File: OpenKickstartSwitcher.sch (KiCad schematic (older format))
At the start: 12 parts, among them J1 Conn_01x03, J2 Conn_01x03, J99 OSHW_LOGO, U1 KS_SOCKET, U2 M27C800, U3 7400

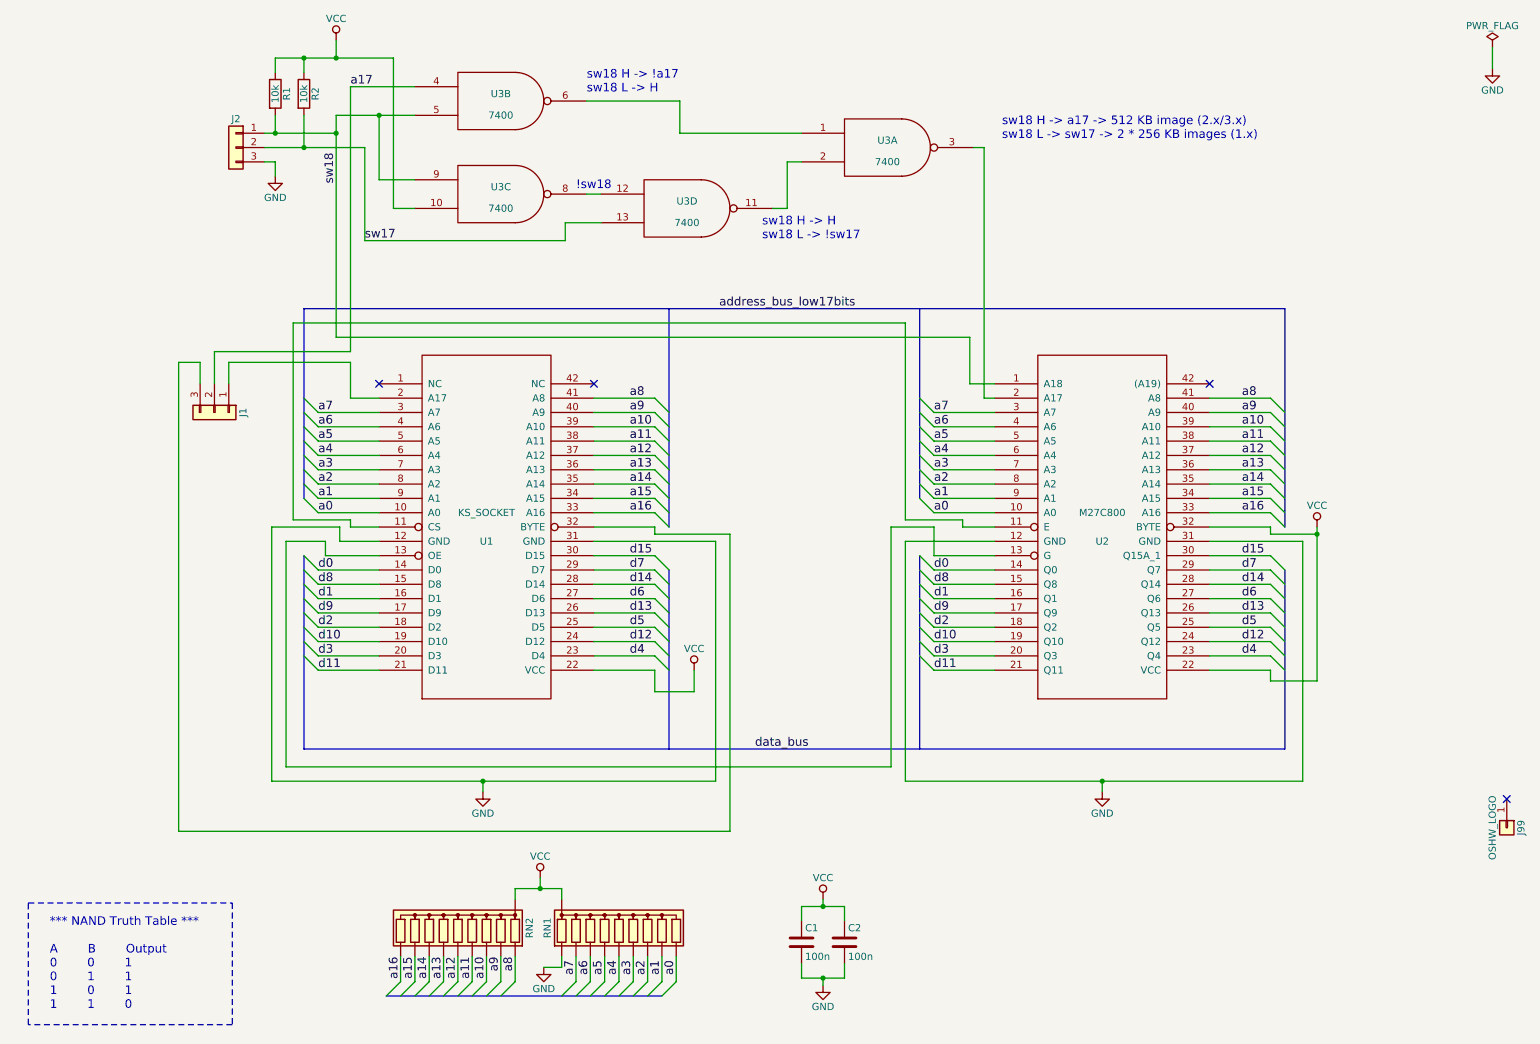
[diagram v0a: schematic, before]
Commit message: Tentative schematics for 5-kickstart version PCB NOT YET UPDATED
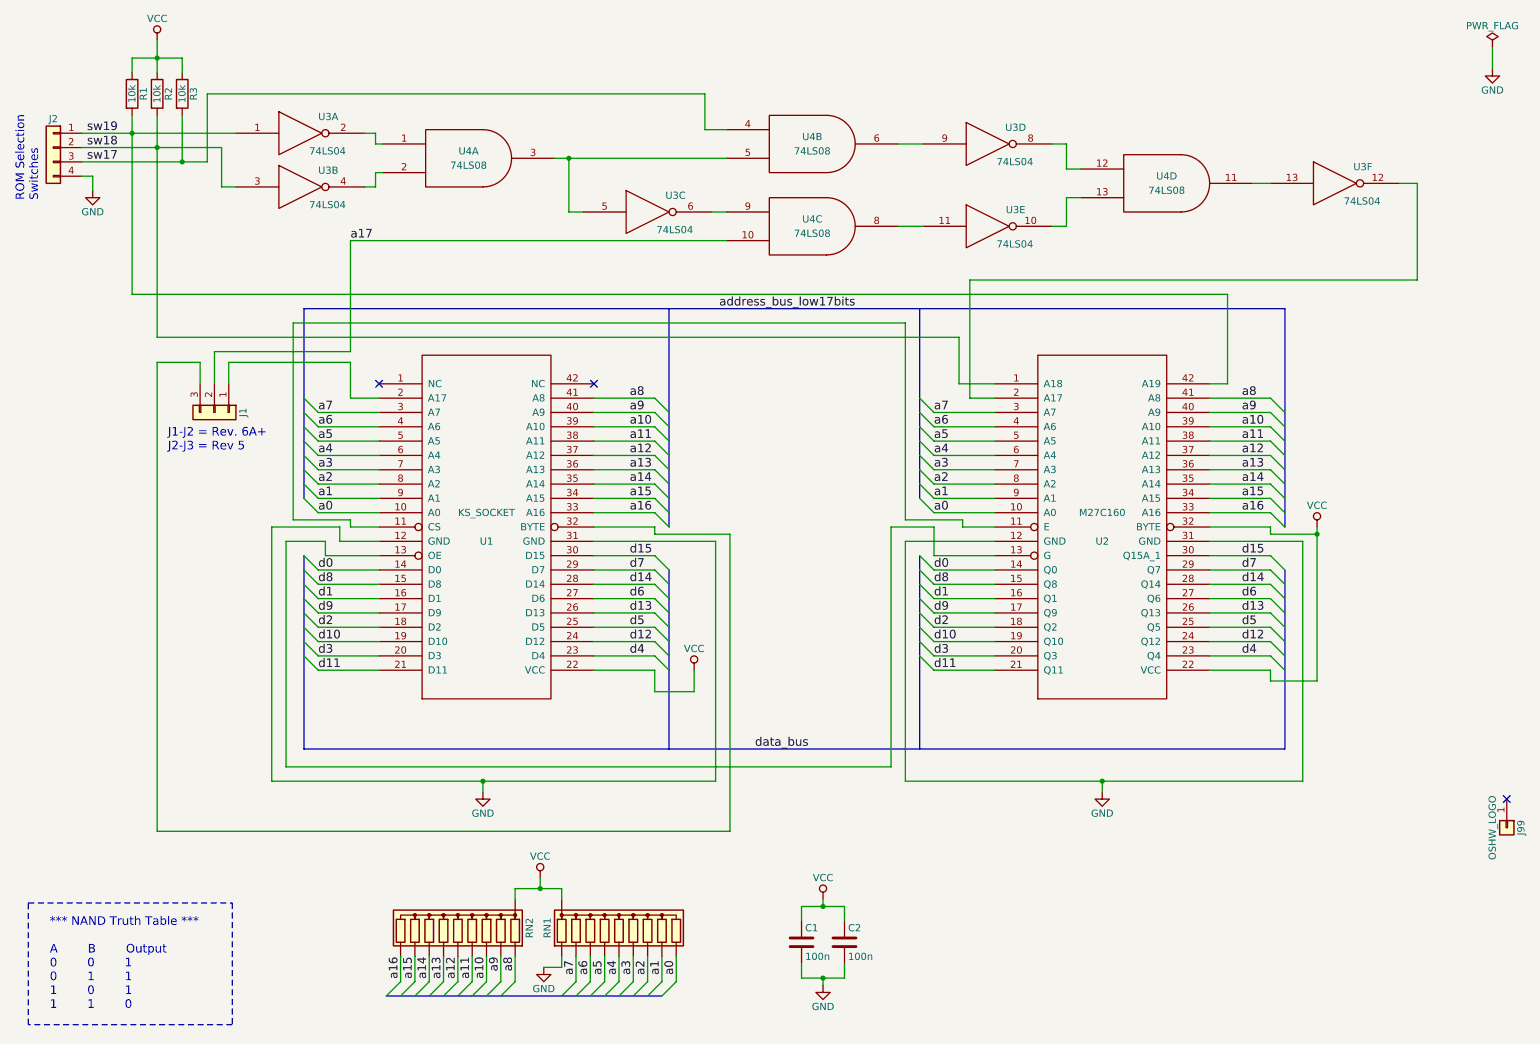
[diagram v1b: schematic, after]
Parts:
- removed J2: Conn_01x03, OpenKickstartSwitcher:LoosePads-3, symbol Conn_01x03
- removed U2: M27C800, OpenKickstartSwitcher:DIP-42_Socket, symbol M27C800
- removed U3: 7400, Housings_DIP:DIP-14_W7.62mm, symbol 7400
- added J2: Conn_01x04, symbol Conn_01x04
- added R3: 10k, Resistors_THT:R_Axial_DIN0207_L6.3mm_D2.5mm_P10.16mm_Horizontal, symbol R
- added U2: M27C160, MODULE, symbol M27C160
- added U3: 74LS04, symbol 74LS04
- added U4: 74LS08, symbol 74LS08
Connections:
- net GND: now also J2.4 (Pin_4), U2.12 (GND), U2.31 (GND), U3.7 (GND), U3.7 (GND), U3.7 (GND), U3.7 (GND), U3.7 (GND), U3.7 (GND), U4.7 (GND), U4.7 (GND), U4.7 (GND), U4.7 (GND)
- net VCC: now also R3.1, U2.22 (VCC), U2.32 (BYTE), U3.14 (VCC), U3.14 (VCC), U3.14 (VCC), U3.14 (VCC), U3.14 (VCC), U3.14 (VCC), U4.14 (VCC), U4.14 (VCC), U4.14 (VCC), U4.14 (VCC)
- net a0: now also U2.10 (A0)
- net a1: now also U2.9 (A1)
- net a10: now also U2.39 (A10)
- net a11: now also U2.38 (A11)
- net a12: now also U2.37 (A12)
- net a13: now also U2.36 (A13)
- net a14: now also U2.35 (A14)
- net a15: now also U2.34 (A15)
- net a16: now also U2.33 (A16)
- net a17: now also U4.10
- net a2: now also U2.8 (A2)
- net a3: now also U2.7 (A3)
- net a4: now also U2.6 (A4)
- net a5: now also U2.5 (A5)
- net a6: now also U2.4 (A6)
- net a7: now also U2.3 (A7)
- net a8: now also U2.41 (A8)
- net a9: now also U2.40 (A9)
- net d0: now also U2.14 (Q0)
- net d1: now also U2.16 (Q1)
- net d10: now also U2.19 (Q10)
- net d11: now also U2.21 (Q11)
- net d12: now also U2.24 (Q12)
- net d13: now also U2.26 (Q13)
- net d14: now also U2.28 (Q14)
- net d15: now also U2.30 (Q15A_1)
- net d2: now also U2.18 (Q2)
- net d3: now also U2.20 (Q3)
- net d4: now also U2.23 (Q4)
- net d5: now also U2.25 (Q5)
- net d6: now also U2.27 (Q6)
- net d7: now also U2.29 (Q7)
- net d8: now also U2.15 (Q8)
- net d9: now also U2.17 (Q9)
- net sw17: now also J2.3 (Pin_3), R3.2, U4.4; no longer R2.2
- net sw18: now also R2.2, J2.2 (Pin_2), U2.1 (A18), U3.3; no longer R1.2
- net at U1.11 (CS): now also U2.11 (E)
- net at U1.13 (OE): now also U2.13 (G)
- new net: U3.2, U4.1
- new net: U3.4, U4.2
- new net: U3.5, U4.3, U4.5
- new net: U3.6, U4.9
- new net: U3.8, U4.12
- new net: U3.9, U4.6
- new net: U3.10, U4.13
- new net: U3.11, U4.8
- new net: U2.2 (A17), U3.12
- new net: U3.13, U4.11
- new net sw19: J2.1 (Pin_1), R1.2, U2.42 (A19), U3.1
- no-connect marks 4 -> 3
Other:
- note added: "J1-J2 = Rev. 6A+\nJ2-J3 = Rev 5"
- note added: "ROM Selection\nSwitches"
- note removed: "!sw18"
- note removed: "sw18 H -> !a17\nsw18 L -> H"
- note removed: "sw18 H -> H\nsw18 L -> !sw17"
- note removed: "sw18 H -> a17 -> 512 KB image (2.x/3.x)\nsw18 L -> sw17 -> 2 * 256 KB images (1.x)"
- moved on the sheet: R1, R2

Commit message: Update schematics
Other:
- note removed: "*** NAND Truth Table ***\n\nA B Output\n0 0 1\n0 1 1\n1 0 1\n1 1 0"
- moved on the sheet: J1, J2, R1, R2, R3, U1, U2, U3A, U3B, U3C, U3D, U3E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

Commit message: WIP
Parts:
- added C3: 100n, Capacitors_THT:C_Disc_D7.0mm_W2.5mm_P5.00mm, symbol C
- J2: footprint (none) -> OpenKickstartSwitcher:LoosePads-4
- R1, R2, R3: footprint Resistors_THT:R_Axial_DIN0207_L6.3mm_D2.5mm_P10.16mm_Horizontal -> Resistors_THT:R_Axial_DIN0207_L6.3mm_D2.5mm_P7.62mm_Horizontal
- U2: footprint MODULE -> OpenKickstartSwitcher:DIP-42_Socket
- U3, U4: footprint (none) -> Housings_DIP:DIP-14_W7.62mm
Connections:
- net GND: now also J2.1 (Pin_1), C3.2; no longer J2.4 (Pin_4)
- net VCC: now also C3.1
- net a17: now also U4.5; no longer U4.10
- net sw17: now also J2.2 (Pin_2), U4.9; no longer J2.3 (Pin_3), U4.4
- net sw18: now also J2.3 (Pin_3), U3.9; no longer J2.2 (Pin_2), U3.3
- net sw19: now also J2.4 (Pin_4), U3.5; no longer J2.1 (Pin_1), U3.1
- net at U3.2: now also U4.12; no longer U4.1
- net at U3.4: now also U4.4; no longer U4.2
- net at U3.6: now also U4.1; no longer U4.9
- net at U3.8: now also U4.2; no longer U4.12
- net at U4.6: now also U3.11; no longer U3.9
- net at U4.8: now also U3.1; no longer U3.11
- new net: U3.3, U4.10, U4.3
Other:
- moved on the sheet: C1, C2, RN1, RN2, U3A, U3B, U3C, U3D, U4B, U4C
